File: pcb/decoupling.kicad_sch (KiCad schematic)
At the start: 84 parts

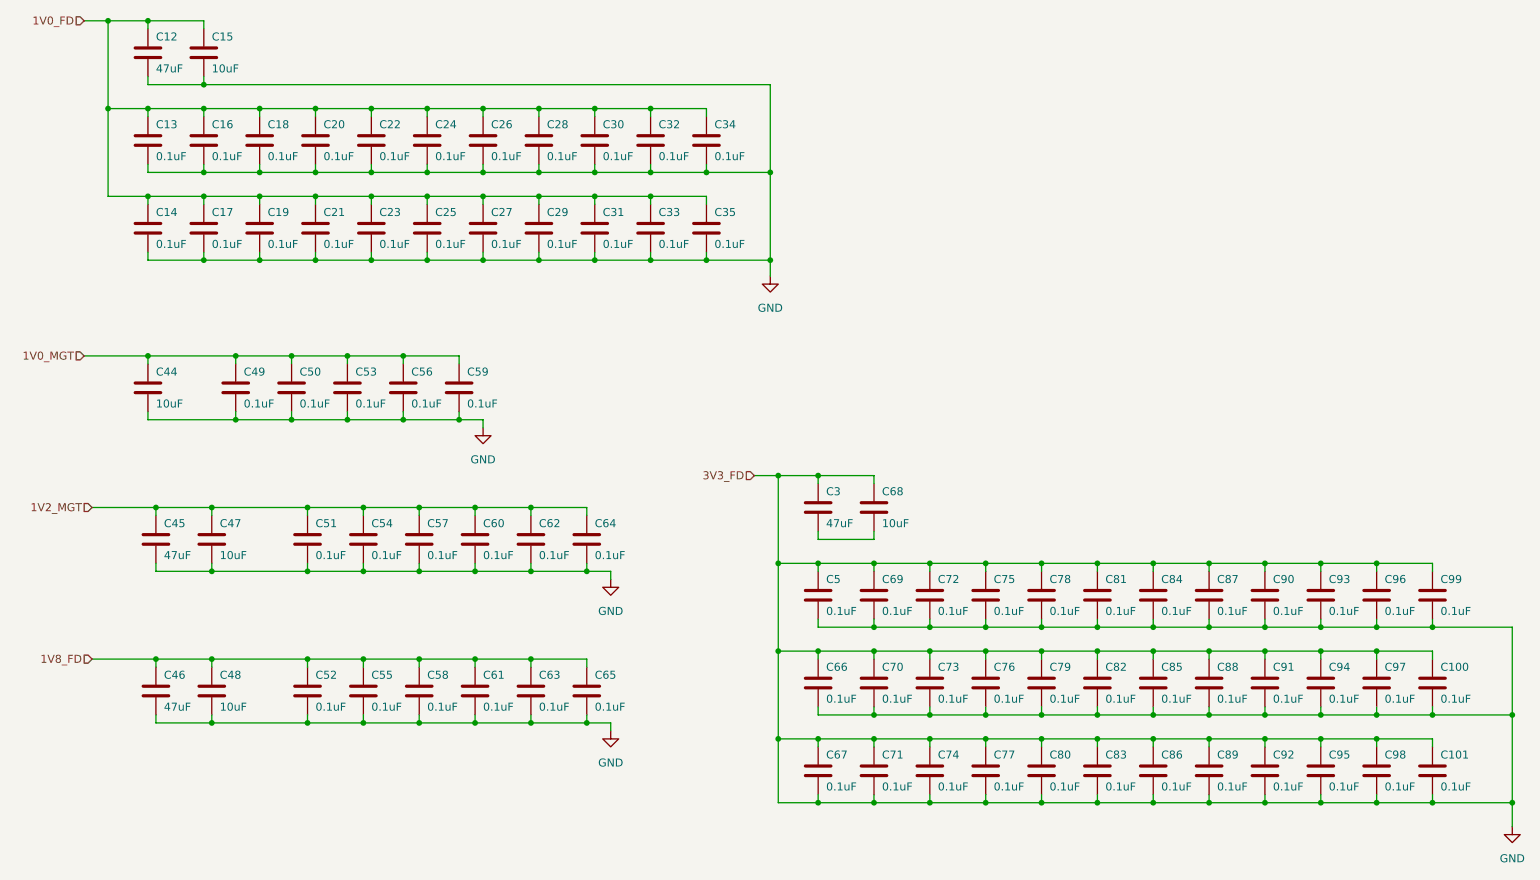
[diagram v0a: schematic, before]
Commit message: defined memory pinouts
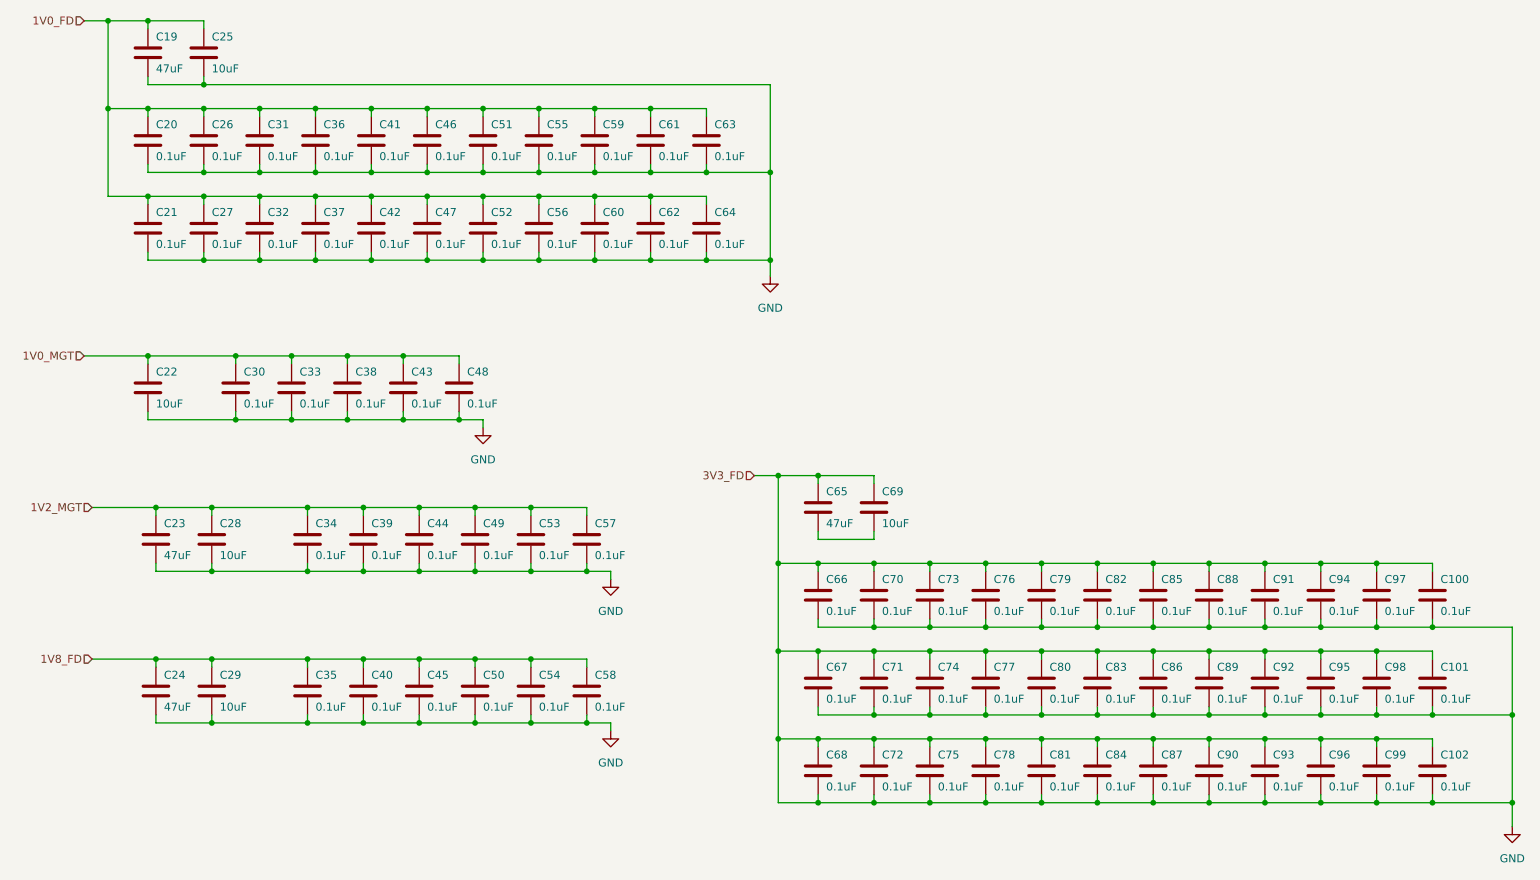
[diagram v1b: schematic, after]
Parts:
- renumbered C99 to C100, C100 to C101, C101 to C102, C12 to C19, C13 to C20, C14 to C21, C44 to C22, C45 to C23, C46 to C24, C15 to C25, C16 to C26, C17 to C27, C47 to C28, C48 to C29, C49 to C30, C18 to C31, C19 to C32, C50 to C33, C51 to C34, C52 to C35, C20 to C36, C21 to C37, C53 to C38, C54 to C39, C55 to C40, C22 to C41, C23 to C42, C56 to C43, C57 to C44, C58 to C45, C24 to C46, C25 to C47, C59 to C48, C60 to C49, C61 to C50, C26 to C51, C27 to C52, C62 to C53, C63 to C54, C28 to C55, C29 to C56, C64 to C57, C65 to C58, C30 to C59, C31 to C60, C32 to C61, C33 to C62, C34 to C63, C35 to C64, C3 to C65, C5 to C66, C66 to C67, C67 to C68, C68 to C69, C69 to C70, C70 to C71, C71 to C72, C72 to C73, C73 to C74, C74 to C75, C75 to C76, C76 to C77, C77 to C78, C78 to C79, C79 to C80, C80 to C81, C81 to C82, C82 to C83, C83 to C84, C84 to C85, C85 to C86, C86 to C87, C87 to C88, C88 to C89, C89 to C90, C90 to C91, C91 to C92, C92 to C93, C93 to C94, C94 to C95, C95 to C96, C96 to C97, C97 to C98, C98 to C99

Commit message: moved stuff around, bom
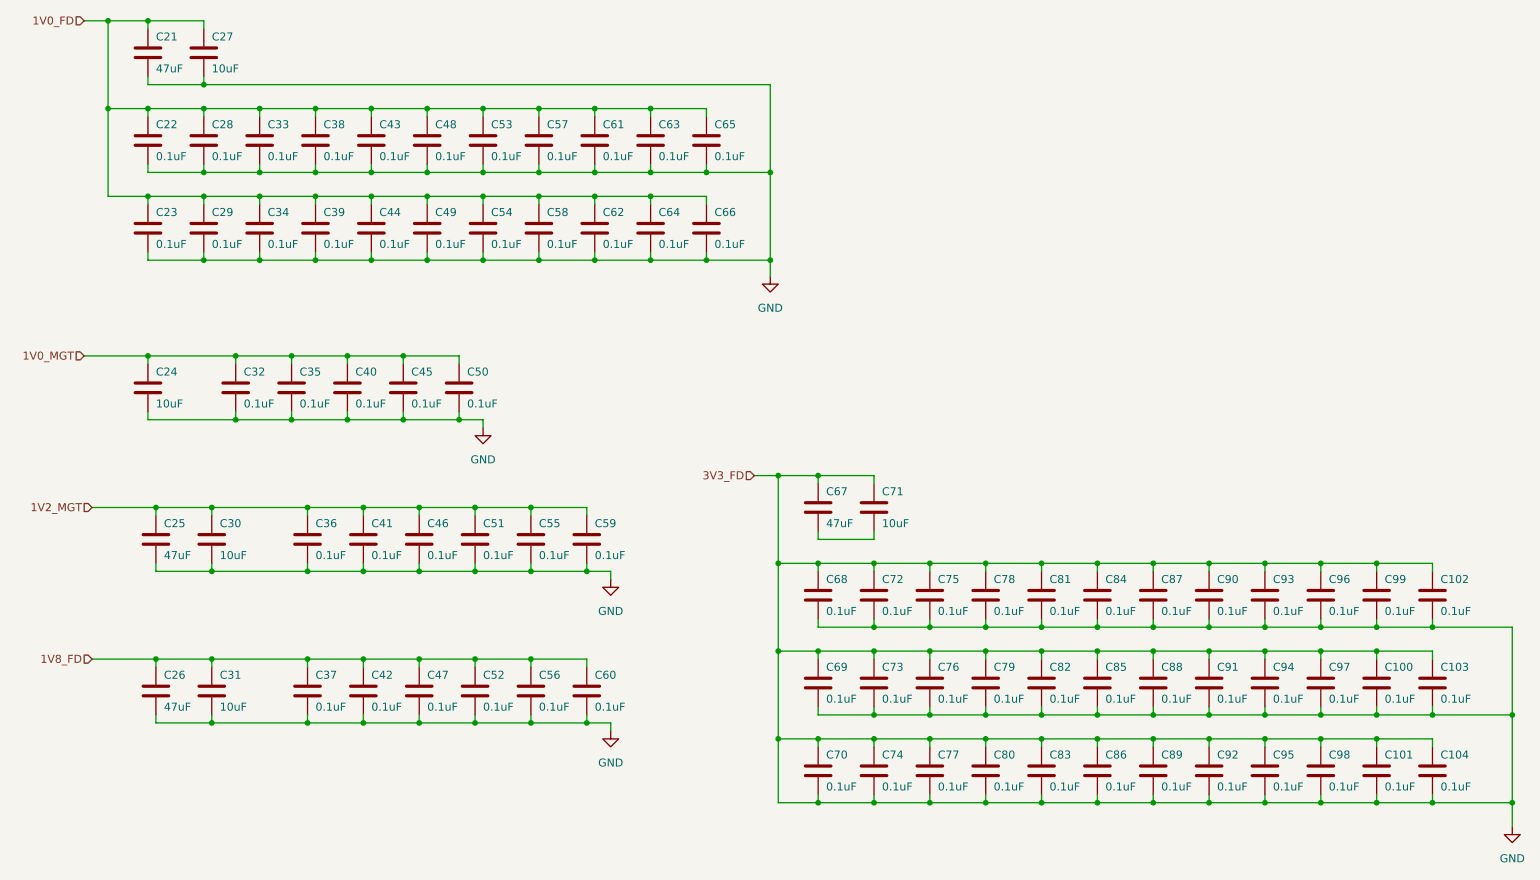
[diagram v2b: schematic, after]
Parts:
- renumbered C98 to C100, C99 to C101, C100 to C102, C101 to C103, C102 to C104, C19 to C21, C20 to C22, C21 to C23, C22 to C24, C23 to C25, C24 to C26, C25 to C27, C26 to C28, C27 to C29, C28 to C30, C29 to C31, C30 to C32, C31 to C33, C32 to C34, C33 to C35, C34 to C36, C35 to C37, C36 to C38, C37 to C39, C38 to C40, C39 to C41, C40 to C42, C41 to C43, C42 to C44, C43 to C45, C44 to C46, C45 to C47, C46 to C48, C47 to C49, C48 to C50, C49 to C51, C50 to C52, C51 to C53, C52 to C54, C53 to C55, C54 to C56, C55 to C57, C56 to C58, C57 to C59, C58 to C60, C59 to C61, C60 to C62, C61 to C63, C62 to C64, C63 to C65, C64 to C66, C65 to C67, C66 to C68, C67 to C69, C68 to C70, C69 to C71, C70 to C72, C71 to C73, C72 to C74, C73 to C75, C74 to C76, C75 to C77, C76 to C78, C77 to C79, C78 to C80, C79 to C81, C80 to C82, C81 to C83, C82 to C84, C83 to C85, C84 to C86, C85 to C87, C86 to C88, C87 to C89, C88 to C90, C89 to C91, C90 to C92, C91 to C93, C92 to C94, C93 to C95, C94 to C96, C95 to C97, C96 to C98, C97 to C99

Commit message: jtag, dcplng
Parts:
- removed C25: 47uF, Capacitor_SMD:C_0603_1608Metric, symbol library:C
- removed C30: 10uF, Capacitor_SMD:C_0402_1005Metric, symbol library:C
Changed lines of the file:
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@@
-	(symbol
-		(lib_id "library:C")
-		(at 46.99 109.22 0)
-		(unit 1)
-		(exclude_from_sim no)
-		(in_bom yes)
-		(on_board yes)
-		(dnp no)
-		(property "Reference" "C25"
-			(at 48.26 106.68 0)
-			(effects
-				(font
-					(size 1.27 1.27)
-				)
-				(justify left)
-			)
-		)
-		(property "Value" "47uF"
-			(at 48.26 111.76 0)
-			(effects
-				(font
-					(size 1.27 1.27)
-				)
-				(justify left)
-			)
-		)
-		(property "Footprint" "Capacitor_SMD:C_0603_1608Metric"
-			(at 47.9552 113.03 0)
-			(effects
-				(font
-					(size 1.27 1.27)
-				)
-				(hide yes)
-			)
-		)
-		(property "Datasheet" "~"
-			(at 46.99 109.22 0)
-			(effects
-				(font
-					(size 1.27 1.27)
-				)
-				(hide yes)
-			)
-		)
-		(property "Description" "Unpolarized capacitor"
-			(at 46.99 109.22 0)
-			(effects
-				(font
-					(size 1.27 1.27)
-				)
-				(hide yes)
-			)
-		)
-		(property "Name" ""
-			(at 46.99 109.22 0)
-			(effects
-				(font
-					(size 1.27 1.27)
-				)
-				(hide yes)
-			)
-		)
-		(pin "1"
-		)
-		(pin "2"
-		)
-		(instances
-			(project "RPi-HwAB-1"
-				(path "/e63e39d7-6ac0-4ffd-8aa3-1841a4541b55/59d21473-a004-4514-8090-fd93db818925/94db1840-7840-4b32-9939-76c2575d480c/d1fe51bb-390e-4bc5-afb0-b85902b013c3"
-					(reference "C25")
-					(unit 1)
-				)
-			)
-		)
-	)
 	(symbol
 		(lib_id "library:C")
@@
 					(unit 1)
 				)
-			)
-		)
-	)
-	(symbol
-		(lib_id "library:C")
-		(at 55.88 109.22 0)
-		(unit 1)
-		(exclude_from_sim no)
-		(in_bom yes)
-		(on_board yes)
-		(dnp no)
-		(property "Reference" "C30"
-			(at 57.15 106.68 0)
-			(effects
-				(font
-					(size 1.27 1.27)
-				)
-				(justify left)
-			)
-		)
-		(property "Value" "10uF"
-			(at 57.15 111.76 0)
-			(effects
-				(font
-					(size 1.27 1.27)
-				)
-				(justify left)
-			)
-		)
-		(property "Footprint" "Capacitor_SMD:C_0402_1005Metric"
-			(at 56.8452 113.03 0)
-			(effects
-				(font
-					(size 1.27 1.27)
-				)
-				(hide yes)
-			)
-		)
-		(property "Datasheet" "~"
-			(at 55.88 109.22 0)
-			(effects
-				(font
-					(size 1.27 1.27)
-				)
-				(hide yes)
-			)
-		)
-		(property "Description" "Unpolarized capacitor"
-			(at 55.88 109.22 0)
-			(effects
-				(font
-					(size 1.27 1.27)
-				)
-				(hide yes)
-			)
-		)
-		(property "Name" ""
-			(at 55.88 109.22 0)
-			(effects
-				(font
-					(size 1.27 1.27)
-				)
-				(hide yes)
-			)
-		)
-		(pin "1"
-		)
-		(pin "2"
-		)
-		(instances
-			(project "RPi-HwAB-1"
-				(path "/e63e39d7-6ac0-4ffd-8aa3-1841a4541b55/59d21473-a004-4514-8090-fd93db818925/94db1840-7840-4b32-9939-76c2575d480c/d1fe51bb-390e-4bc5-afb0-b85902b013c3"
-					(reference "C30")
-					(unit 1)
-				)
